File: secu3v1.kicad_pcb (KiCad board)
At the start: 2 copper layers, 80 x 95 mm, 190 parts, among them IC1 ATMEGA1284-A, P1 HCCPHPE24BKA90, P2 CONN_01X16, P3 CONN_02X03, Q1 BC817, Q10 BC817, Q11 BC817, Q12 BC817, Q13 BC817, Q14 BC817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

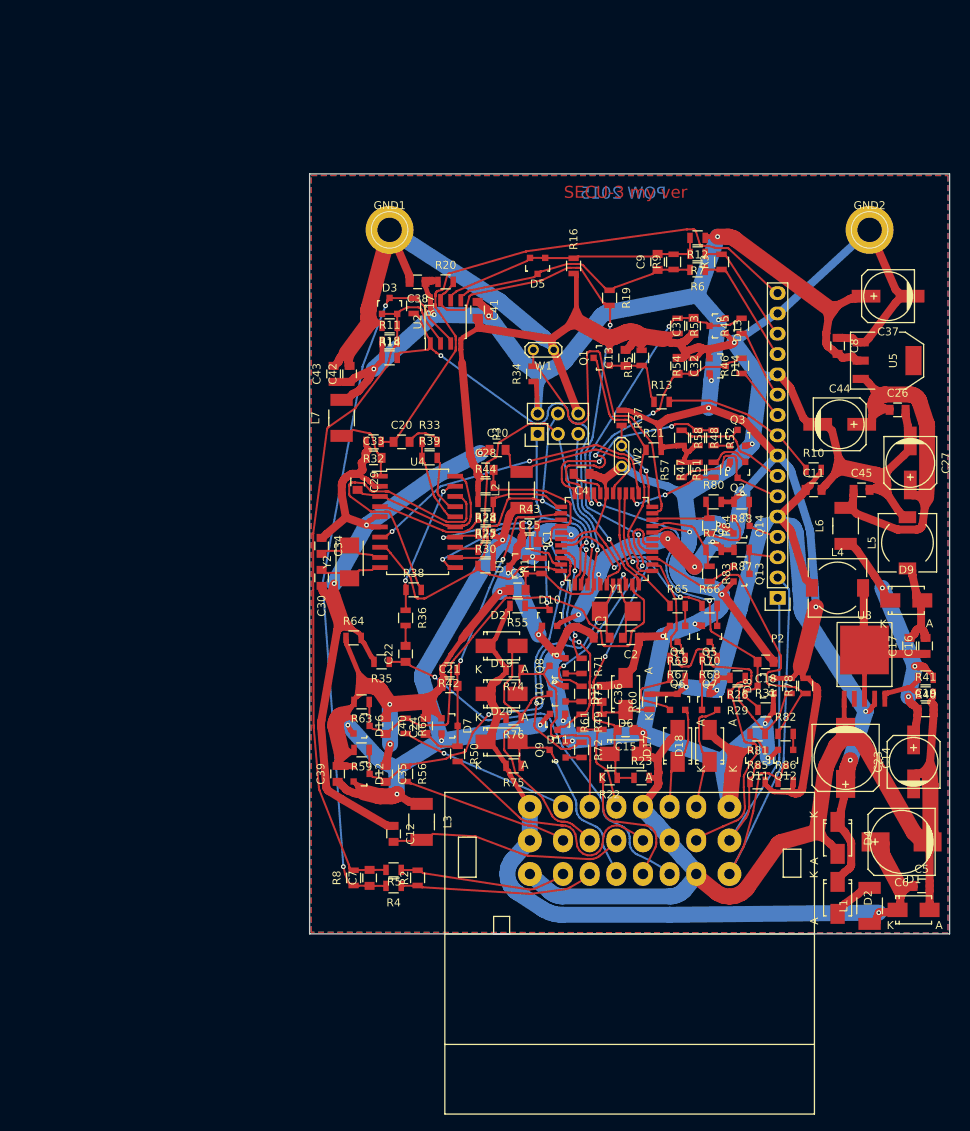
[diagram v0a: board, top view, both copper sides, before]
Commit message: промежуточная точка - исправлено размещение отверстий и платы в корпусе
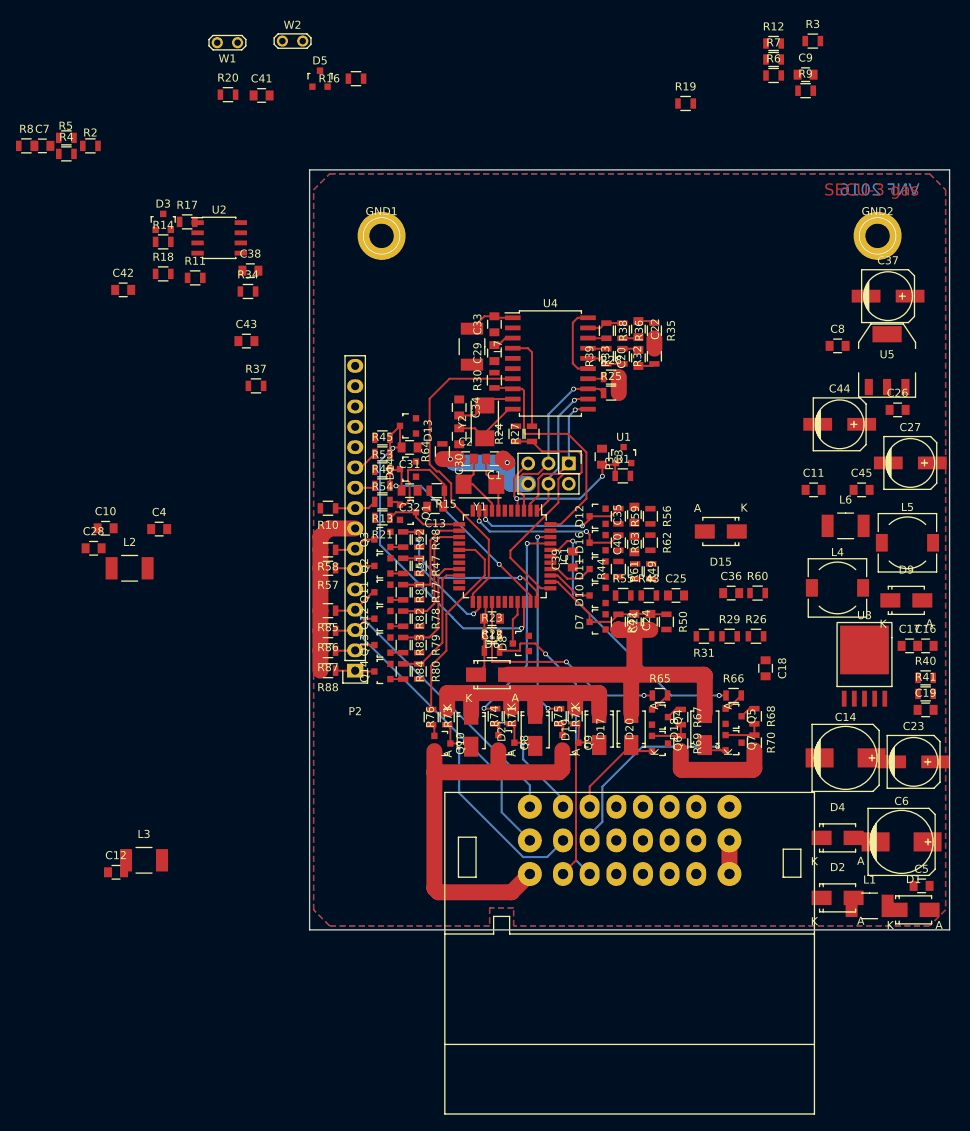
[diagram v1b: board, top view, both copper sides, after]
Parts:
- moved C7 100.2 mm to (26.6, 44.5), turned to 0 degrees
- moved R2 100.2 mm to (32.6, 44.5), turned to 0 degrees
- moved R4 100.2 mm to (29.6, 45.5), turned to 0 degrees
- moved R5 100.2 mm to (29.6, 43.5), turned to 0 degrees
- moved R8 100.2 mm to (24.6, 44.5), turned to 0 degrees
- moved W2 66.0 mm to (56.6, 31.4), turned to 0 degrees
- moved R10 60.9 mm to (62.3, 89.8), turned to 180 degrees
- moved R86 60.2 mm to (62.3, 105.1), turned to 180 degrees
- moved R85 57.8 mm to (62.3, 102.6), turned to 180 degrees
- moved R88 55.8 mm to (62.3, 110.1)
- moved W1 55.1 mm to (51.0, 31.6)
- moved R35 53.6 mm to (103.1, 67.6), turned to 270 degrees
- moved P2 53.6 mm to (65.7, 110.1)
- moved Q12 53.3 mm to (69.1, 103.6), turned to 90 degrees
- moved C4 53.2 mm to (41.2, 92.4), turned to 0 degrees
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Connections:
- P1 pad 1B: IGN_OUT1 -> +VS
- P1 pad 1C: IGN_OUT2 -> +VS
- P1 pad 2A: IE_OUT -> RX_IN
- P1 pad 3A: FE_OUT -> TX_OUT
- P1 pad 4C: GAS -> sync1+
- P1 pad 5C: CE_OUT -> sync1-
- P1 pad 6A: STB_OUT -> FE_OUT
- P1 pad 6B: FAN_OUT -> IE_OUT
- P1 pad 6C: sync1+ -> GAS
- P1 pad 7A: TX_OUT -> STB_OUT
- P1 pad 7B: RX_IN -> FAN_OUT
- P1 pad 7C: sync1- -> CE_OUT
- P1 pad 8A: +VS -> IGN_OUT1
- P1 pad 8B: +VS -> IGN_OUT2
- P2 pad 1: IGN_OUT1 -> IGN_OUT4
- P2 pad 2: IGN_OUT2 -> IGN_OUT3
- P2 pad 3: IGN_OUT3 -> IGN_OUT2
- P2 pad 4: IGN_OUT4 -> IGN_OUT1
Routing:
- net GND: track 759.7 -> 110.4 mm, vias 20 -> 2
- net +5V: track 410.1 -> 23.5 mm, vias 21 -> 0
- net GNDA: track 106.8 -> 1.30 mm, vias 3 -> 0
- net +12V: track 115.2 -> 13.8 mm, vias 4 -> 0
- net Net-(C7-Pad1): track 89.8 -> 0.00 mm, vias 2 -> 0
- net Net-(C7-Pad2): track 88.5 -> 0.00 mm
- net +VS: track 113.0 -> 37.0 mm, vias 1 -> 0
- net KS2: track 71.9 -> 2.10 mm
- net Net-(IC1-Pad15): track 65.1 -> 0.00 mm, vias 2 -> 0
- net Net-(IC1-Pad11): track 58.2 -> 0.00 mm, vias 2 -> 0
- net +6V: track 57.9 -> 0.00 mm
- net Net-(IC1-Pad21): track 46.9 -> 0.00 mm
- net KS1: track 48.7 -> 2.10 mm, vias 1 -> 0
- net Net-(C28-Pad2): track 46.6 -> 5.90 mm, vias 2 -> 0
- net TXD: track 60.0 -> 21.2 mm, vias 0 -> 2
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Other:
- outline, holes or cut-outs redrawn
- board text added: "SECU-3 gas"
- board text added: "VNF 2016"
- board text removed: "POW 2015"
- board text removed: "SECU-3 my ver"
